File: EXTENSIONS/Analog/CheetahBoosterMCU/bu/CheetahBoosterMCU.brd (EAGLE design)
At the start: 50 x 79 mm, 11 parts

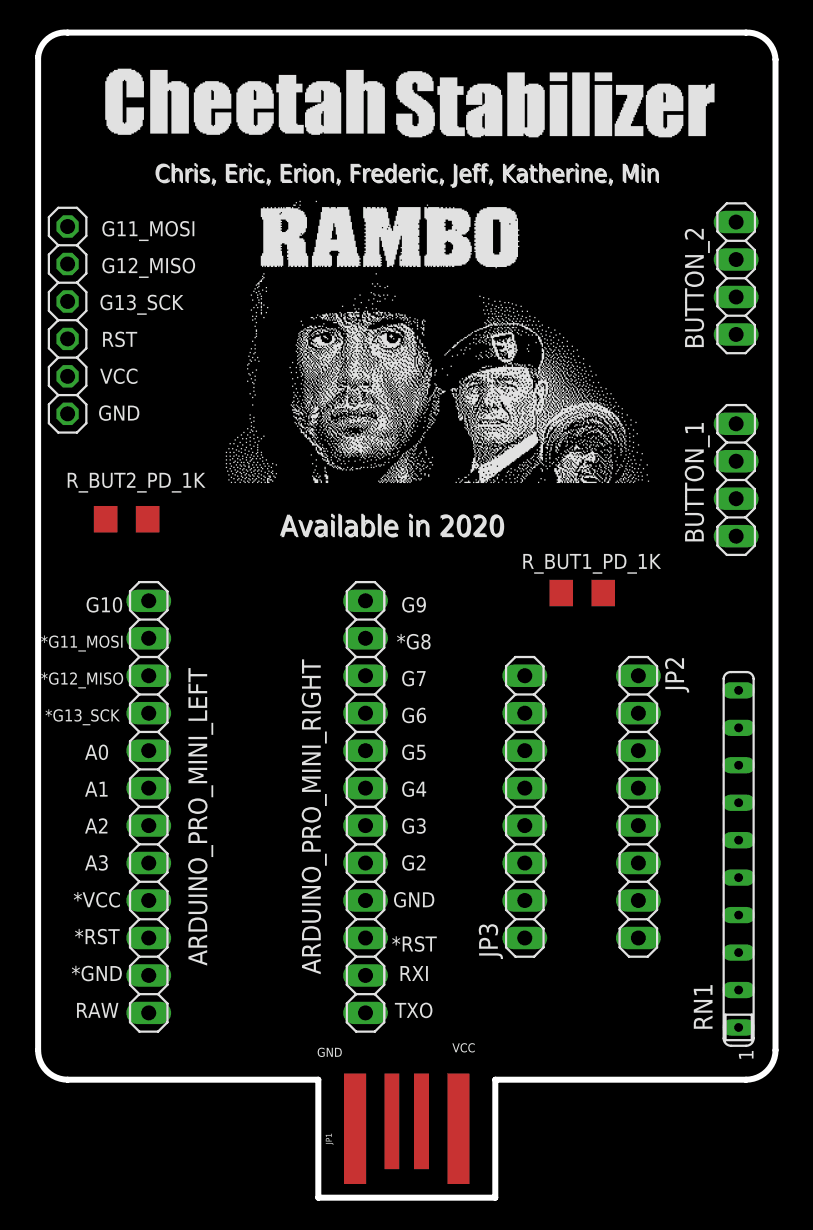
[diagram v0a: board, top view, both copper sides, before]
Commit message: Create CheetahBooster MCU
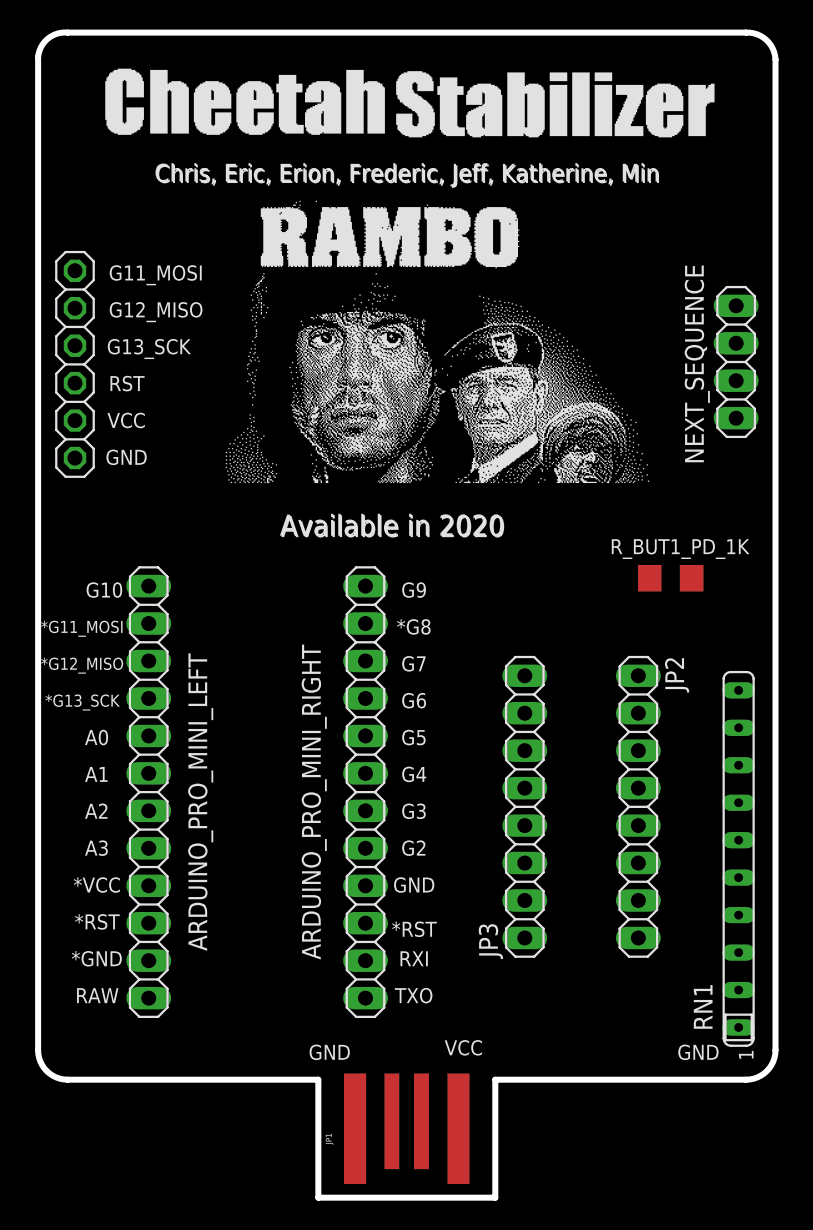
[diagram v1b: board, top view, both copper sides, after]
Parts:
- removed BUTTON_1, BUTTON_2: (no value), pinhead:1X04
- removed R_BUT2_PD_1K: (no value), adafruit:R1206
- added NEXT_SEQUENCE: (no value), pinhead:1X04
- moved R_BUT1_PD_1K 6.08 mm to (42.9, 43.0)
- moved JP_PROGRAMMING 3.04 mm to (2.50, 57.5)
- moved ARDUINO_PRO_MINI_LEFT 1.00 mm to (7.50, 28.5)
- moved ARDUINO_PRO_MINI_RIGHT 1.00 mm to (22.2, 28.5)
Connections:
- net A1: no longer BUTTON_2.4, R_BUT2_PD_1K.2
- net A2: now also NEXT_SEQUENCE.4; no longer BUTTON_1.4
- net GND: no longer R_BUT2_PD_1K.1
- net VCC: now also NEXT_SEQUENCE.1; no longer BUTTON_1.1, BUTTON_2.1
